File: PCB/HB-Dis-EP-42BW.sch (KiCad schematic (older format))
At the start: 34 parts, among them J1 Reset, J2 FTDI, J3 Conn_ISP, J4 ePaper, J6 Supply, SW0 SW_Push, SW1 SW_Push, SW10 SW_Push, SW2 SW_Push, SW3 SW_Push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

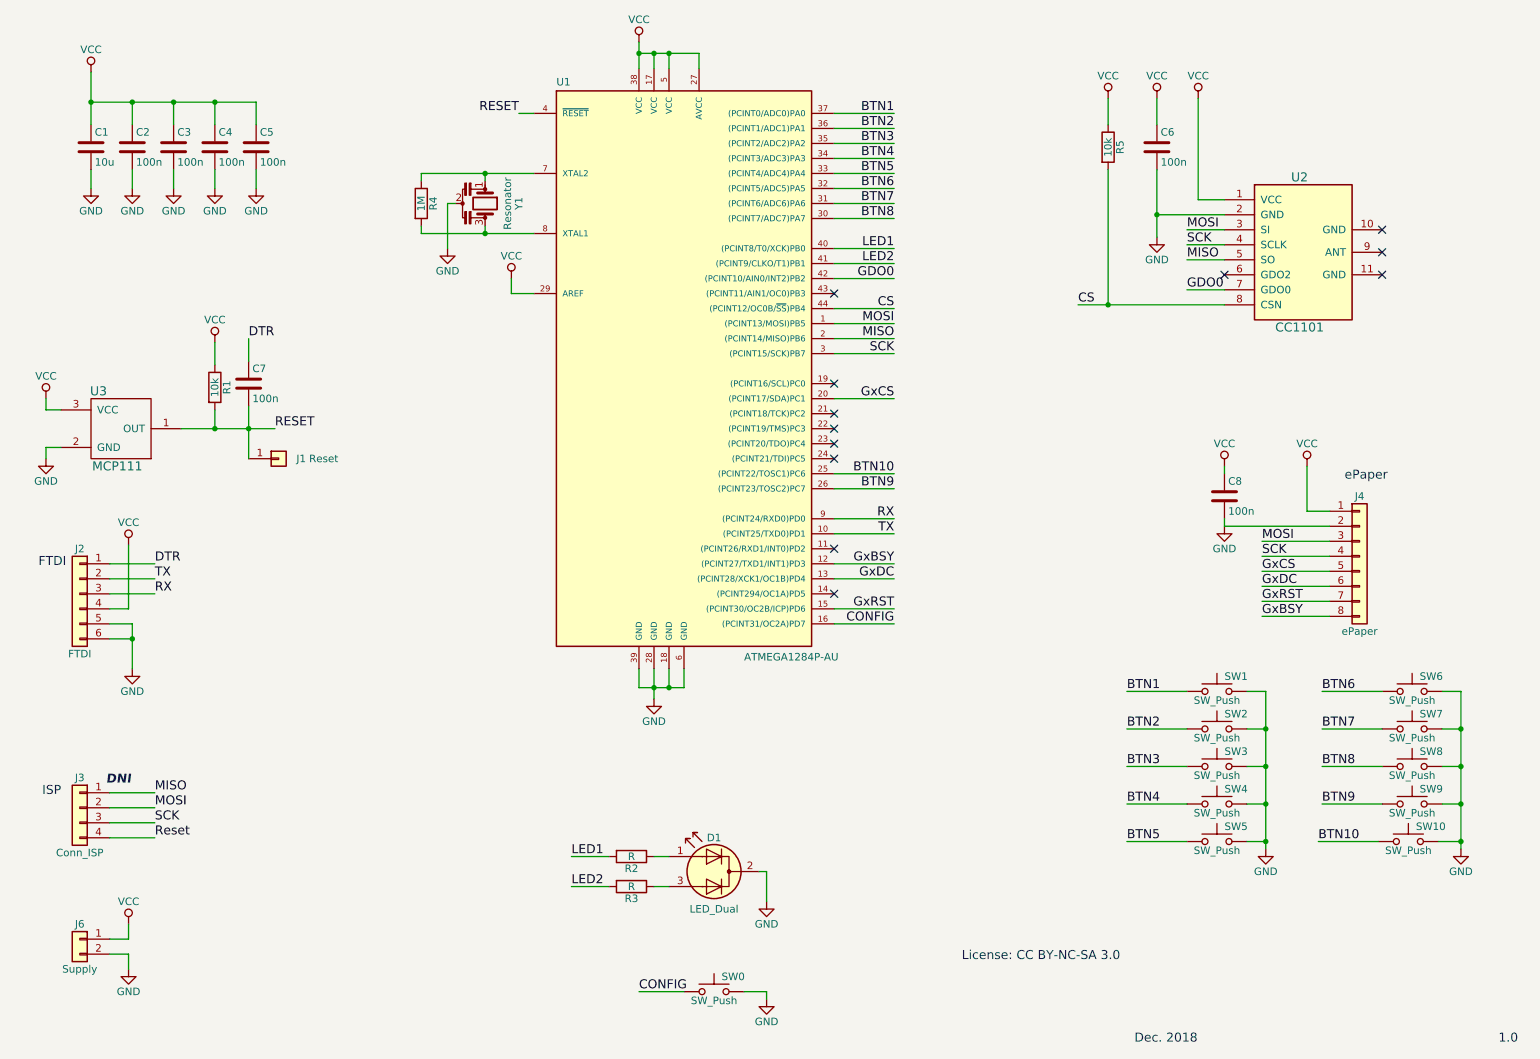
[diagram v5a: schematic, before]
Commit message: several improvement on PCB
- 4x GPIO for future use
- battery measurement under switchable load
- caps @ CC1101 and  @ ePaper changed to 10 uF
- extra solder points on the way to the ePaper connector
  (option to cut the upper 5 mm to fit the size of the bare ePaper)
- remove copper layers in top left, to place antenna there
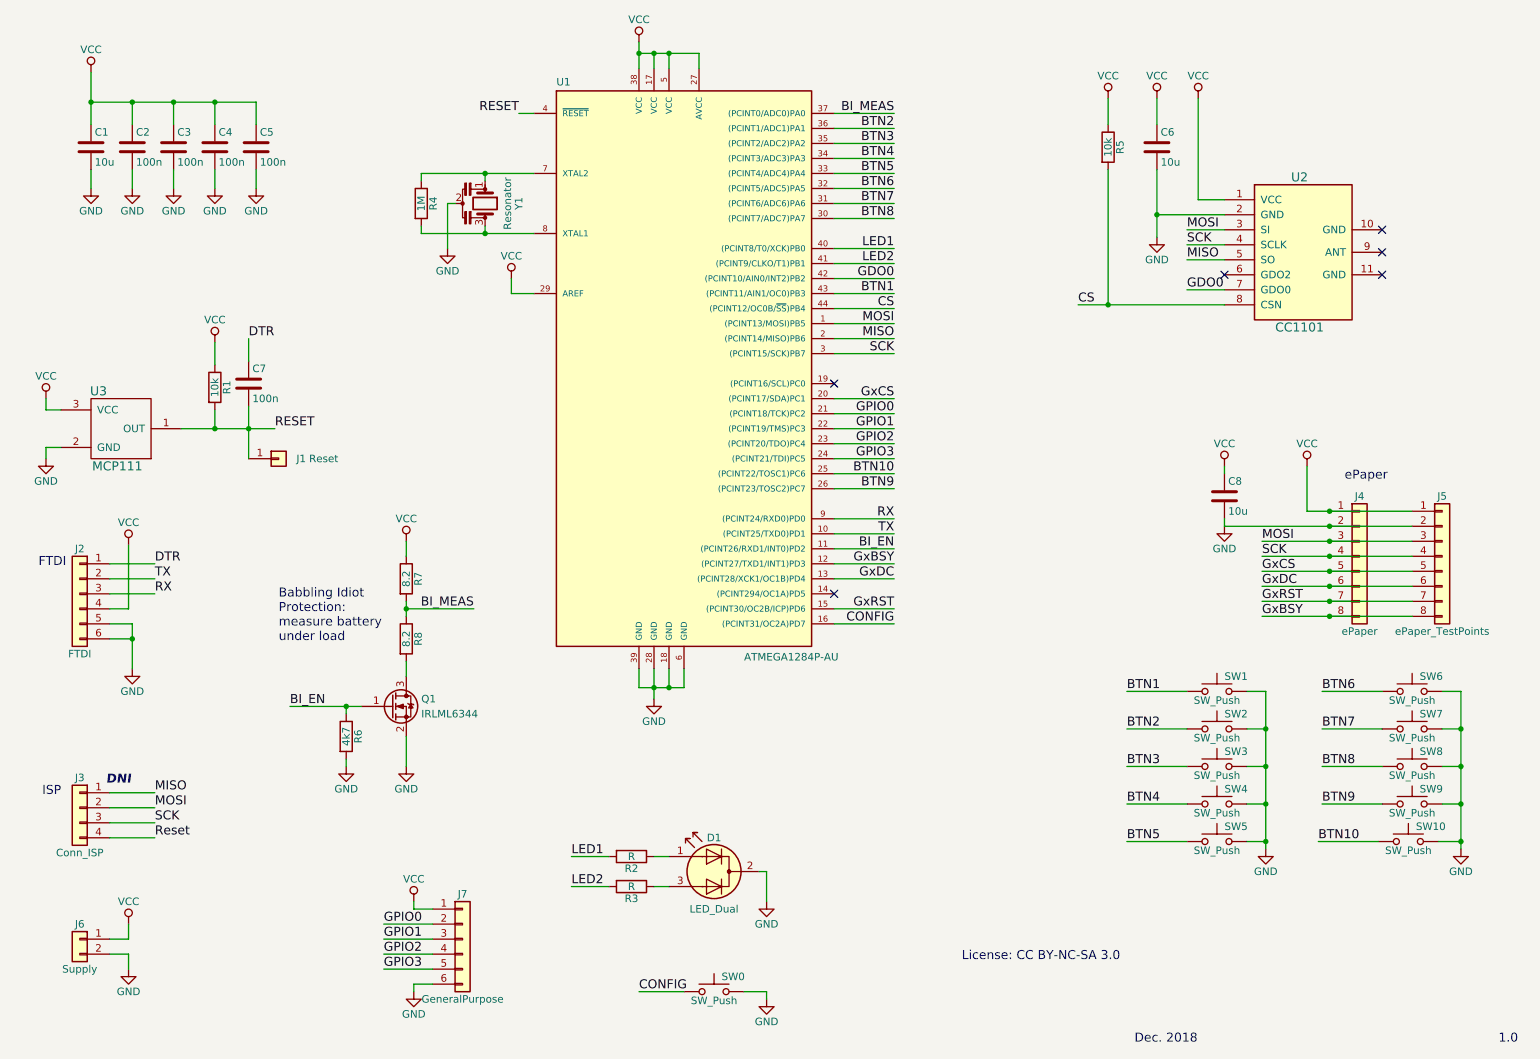
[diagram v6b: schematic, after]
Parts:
- added J5: ePaper_TestPoints, Pin_Headers:Pin_Header_Straight_1x08_Pitch2.54mm, symbol Conn_01x08
- added J7: GeneralPurpose, Pin_Headers:Pin_Header_Straight_1x06_Pitch1.27mm, symbol Conn_01x06
- added Q1: IRLML6344, TO_SOT_Packages_SMD:SOT-23, symbol Q_NMOS_GSD
- added R6: 4k7, Resistors_SMD:R_0603_HandSoldering, symbol R
- added R7, R8: 8.2, Resistors_SMD:R_0603_HandSoldering, symbol R
- C6, C8: value 100n -> 10u
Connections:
- net BTN1: now also U1.43 ((PCINT11/AIN1/OC0)PB3); no longer U1.37 ((PCINT0/ADC0)PA0)
- net GND: now also J5.2 (Pin_2), J7.6 (Pin_6), Q1.2 (S), R6.2
- net GxBSY: now also J5.8 (Pin_8)
- net GxCS: now also J5.5 (Pin_5)
- net GxDC: now also J5.6 (Pin_6)
- net GxRST: now also J5.7 (Pin_7)
- net MOSI: now also J5.3 (Pin_3)
- net SCK: now also J5.4 (Pin_4)
- net VCC: now also J5.1 (Pin_1), J7.1 (Pin_1), R7.1
- net BI_EN: now reaches U1.11 ((PCINT26/RXD1/INT0)PD2)
- net BI_EN: now also Q1.1 (G), R6.1
- net GPIO0: now reaches U1.21 ((PCINT18/TCK)PC2)
- net GPIO0: now also J7.2 (Pin_2)
- net GPIO1: now reaches U1.22 ((PCINT19/TMS)PC3)
- net GPIO1: now also J7.3 (Pin_3)
- net GPIO2: now reaches U1.23 ((PCINT20/TDO)PC4)
- net GPIO2: now also J7.4 (Pin_4)
- net GPIO3: now reaches U1.24 ((PCINT21/TDI)PC5)
- net GPIO3: now also J7.5 (Pin_5)
- new net: Q1.3 (D), R8.2
- new net BI_MEAS: R7.2, R8.1, U1.37 ((PCINT0/ADC0)PA0)
- no-connect marks 12 -> 6
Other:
- note added: "Babbling Idiot \nProtection:\nmeasure battery \nunder load"
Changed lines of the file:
@@
 P 8300 1675
 F 0 "C6" H 8325 1775 50  0000 L CNN
-F 1 "100n" H 8325 1575 50  0000 L CNN
+F 1 "10u" H 8325 1575 50  0000 L CNN
 F 2 "Capacitors_SMD:C_0603_HandSoldering" H 8338 1525 50  0001 C CNN
 F 3 "" H 8300 1675 50  0001 C CNN
@@
 BTN2
 Text Label 6550 1450 2    60   ~ 0
-BTN1
+BI_MEAS
 Text Label 6550 3850 2    60   ~ 0
 BTN10
@@
 Text Label 6550 4750 2    60   ~ 0
 GxRST
-NoConn ~ 6150 2650
-NoConn ~ 6150 3250
-NoConn ~ 6150 3450
-NoConn ~ 6150 3550
-NoConn ~ 6150 3650
-NoConn ~ 6150 3750
-NoConn ~ 6150 4350
 NoConn ~ 6150 4650
 $Comp
@@
 $EndComp
 Wire Wire Line
-	9450 4500 9000 4500
-Wire Wire Line
-	9000 4600 9450 4600
-Wire Wire Line
-	9450 4700 9000 4700
-Wire Wire Line
-	9000 4800 9450 4800
+	9000 4500 10000 4500
+Wire Wire Line
+	9000 4600 10000 4600
+Wire Wire Line
+	9000 4700 10000 4700
+Wire Wire Line
+	9000 4800 10000 4800
 Text Label 9000 4500 0    60   ~ 0
 GxCS
@@
 $EndComp
 Wire Wire Line
-	9450 4200 8750 4200
+	8750 4200 10000 4200
 $Comp
 L VCC #PWR017
@@
 P 8750 4000
 F 0 "C8" H 8775 4100 50  0000 L CNN
-F 1 "100n" H 8775 3900 50  0000 L CNN
+F 1 "10u" H 8775 3900 50  0000 L CNN
 F 2 "Capacitors_SMD:C_0603_HandSoldering" H 8788 3850 50  0001 C CNN
 F 3 "" H 8750 4000 50  0001 C CNN
@@
 	9300 3800 9300 4100
 Wire Wire Line
-	9300 4100 9450 4100
+	9300 4100 10000 4100
 Text Notes 9550 3900 0    60   ~ 0
 ePaper
@@
 $EndComp
 Wire Wire Line
-	9450 4400 9000 4400
-Wire Wire Line
-	9000 4300 9450 4300
+	9000 4400 10000 4400
+Wire Wire Line
+	9000 4300 10000 4300
 Text Label 9000 4300 0    60   ~ 0
 MOSI
@@
 	1    0    0    -1
 $EndComp
+Wire Wire Line
+	6150 3450 6550 3450
+Wire Wire Line
+	6550 3550 6150 3550
+Wire Wire Line
+	6150 3650 6550 3650
+Wire Wire Line
+	6550 3750 6150 3750
+Text Label 6550 3450 2    60   ~ 0
+GPIO0
+Text Label 6550 3550 2    60   ~ 0
+GPIO1
+Text Label 6550 3650 2    60   ~ 0
+GPIO2
+Text Label 6550 3750 2    60   ~ 0
+GPIO3
+$Comp
+L Conn_01x06 J7
+U 1 1 5C3A1225
+P 3675 6950
+F 0 "J7" H 3675 7250 50  0000 C CNN
+F 1 "GeneralPurpose" H 3675 6550 50  0000 C CNN
+F 2 "Pin_Headers:Pin_Header_Straight_1x06_Pitch1.27mm" H 3675 6950 50  0001 C CNN
+F 3 "" H 3675 6950 50  0001 C CNN
+	1    3675 6950
+	1    0    0    -1
+$EndComp
+$Comp
+L GND #PWR029
+U 1 1 5C3A1499
+P 3350 7300
+F 0 "#PWR029" H 3350 7050 50  0001 C CNN
+F 1 "GND" H 3350 7150 50  0000 C CNN
+F 2 "" H 3350 7300 50  0001 C CNN
+F 3 "" H 3350 7300 50  0001 C CNN
+	1    3350 7300
+	1    0    0    -1
+$EndComp
+$Comp
+L VCC #PWR030
+U 1 1 5C3A150D
+P 3350 6700
+F 0 "#PWR030" H 3350 6550 50  0001 C CNN
+F 1 "VCC" H 3350 6850 50  0000 C CNN
+F 2 "" H 3350 6700 50  0001 C CNN
+F 3 "" H 3350 6700 50  0001 C CNN
+	1    3350 6700
+	1    0    0    -1
+$EndComp
+Wire Wire Line
+	3350 7300 3350 7250
+Wire Wire Line
+	3350 7250 3475 7250
+Wire Wire Line
+	3350 6700 3350 6750
+Wire Wire Line
+	3350 6750 3475 6750
+Wire Wire Line
+	3475 6850 3150 6850
+Text Label 3150 6850 0    60   ~ 0
+GPIO0
+Wire Wire Line
+	3475 6950 3150 6950
+Wire Wire Line
+	3475 7050 3150 7050
+Wire Wire Line
+	3150 7150 3475 7150
+Text Label 3150 6950 0    60   ~ 0
+GPIO1
+Text Label 3150 7050 0    60   ~ 0
+GPIO2
+Text Label 3150 7150 0    60   ~ 0
+GPIO3
+$Comp
+L Conn_01x08 J5
+U 1 1 5C3A255F
+P 10200 4400
+F 0 "J5" H 10200 4800 50  0000 C CNN
+F 1 "ePaper_TestPoints" H 10200 3900 50  0000 C CNN
+F 2 "Pin_Headers:Pin_Header_Straight_1x08_Pitch2.54mm" H 10200 4400 50  0001 C CNN
+F 3 "" H 10200 4400 50  0001 C CNN
+	1    10200 4400
+	1    0    0    -1
+$EndComp
+Connection ~ 9450 4100
+Connection ~ 9450 4200
+Connection ~ 9450 4300
+Connection ~ 9450 4400
+Connection ~ 9450 4500
+Connection ~ 9450 4600
+Connection ~ 9450 4700
+Connection ~ 9450 4800
+$Comp
+L Q_NMOS_GSD Q1
+U 1 1 5C3A3284
+P 3200 5400
+F 0 "Q1" H 3400 5450 50  0000 L CNN
+F 1 "IRLML6344" H 3400 5350 50  0000 L CNN
+F 2 "TO_SOT_Packages_SMD:SOT-23" H 3400 5500 50  0001 C CNN
+F 3 "" H 3200 5400 50  0001 C CNN
+	1    3200 5400
+	1    0    0    -1
+$EndComp
+$Comp
+L R R8
+U 1 1 5C3A3483
+P 3300 4950
+F 0 "R8" V 3380 4950 50  0000 C CNN
+F 1 "8.2" V 3300 4950 50  0000 C CNN
+F 2 "Resistors_SMD:R_0603_HandSoldering" V 3230 4950 50  0001 C CNN
+F 3 "" H 3300 4950 50  0001 C CNN
+	1    3300 4950
+	1    0    0    -1
+$EndComp
+$Comp
+L R R7
+U 1 1 5C3A3574
+P 3300 4550
+F 0 "R7" V 3380 4550 50  0000 C CNN
+F 1 "8.2" V 3300 4550 50  0000 C CNN
+F 2 "Resistors_SMD:R_0603_HandSoldering" V 3230 4550 50  0001 C CNN
+F 3 "" H 3300 4550 50  0001 C CNN
+	1    3300 4550
+	1    0    0    -1
+$EndComp
+$Comp
+L GND #PWR031
+U 1 1 5C3A369E
+P 3300 5800
+F 0 "#PWR031" H 3300 5550 50  0001 C CNN
+F 1 "GND" H 3300 5650 50  0000 C CNN
+F 2 "" H 3300 5800 50  0001 C CNN
+F 3 "" H 3300 5800 50  0001 C CNN
+	1    3300 5800
+	1    0    0    -1
+$EndComp
+Wire Wire Line
+	3300 5600 3300 5800
+Wire Wire Line
+	3300 5100 3300 5200
+Wire Wire Line
+	3300 4700 3300 4800
+$Comp
+L VCC #PWR032
+U 1 1 5C3A3BF5
+P 3300 4300
+F 0 "#PWR032" H 3300 4150 50  0001 C CNN
+F 1 "VCC" H 3300 4450 50  0000 C CNN
+F 2 "" H 3300 4300 50  0001 C CNN
+F 3 "" H 3300 4300 50  0001 C CNN
+	1    3300 4300
+	1    0    0    -1
+$EndComp
+Wire Wire Line
+	3300 4300 3300 4400
+$Comp
+L R R6
+U 1 1 5C3A3E02
+P 2900 5600
+F 0 "R6" V 2980 5600 50  0000 C CNN
+F 1 "4k7" V 2900 5600 50  0000 C CNN
+F 2 "Resistors_SMD:R_0603_HandSoldering" V 2830 5600 50  0001 C CNN
+F 3 "" H 2900 5600 50  0001 C CNN
+	1    2900 5600
+	1    0    0    -1
+$EndComp
+Wire Wire Line
+	2525 5400 3000 5400
+Wire Wire Line
+	2900 5450 2900 5400
+Connection ~ 2900 5400
+Wire Wire Line
+	3300 4750 3750 4750
+Connection ~ 3300 4750
+Text Label 2525 5400 0    60   ~ 0
+BI_EN
+Text Label 3750 4750 2    60   ~ 0
+BI_MEAS
+$Comp
+L GND #PWR033
+U 1 1 5C3A45E4
+P 2900 5800
+F 0 "#PWR033" H 2900 5550 50  0001 C CNN
+F 1 "GND" H 2900 5650 50  0000 C CNN
+F 2 "" H 2900 5800 50  0001 C CNN
+F 3 "" H 2900 5800 50  0001 C CNN
+	1    2900 5800
+	1    0    0    -1
+$EndComp
+Wire Wire Line
+	2900 5800 2900 5750
+Text Label 6550 4350 2    60   ~ 0
+BI_EN
+Wire Wire Line
+	6150 2650 6550 2650
+Text Label 6550 2650 2    60   ~ 0
+BTN1
+Text Notes 2450 4975 0    60   ~ 0
+Babbling Idiot \nProtection:\nmeasure battery \nunder load
+Wire Wire Line
+	6150 4350 6550 4350
+NoConn ~ 6150 3250
 $EndSCHEMATC

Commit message: further improvements to PCB
- change caps @ CC1101 and @ ePaper to 1 uF
- shrink GPIOs to 3
- add I²C connecter for future use
- move config button to desired place and add hole for optional head-over-heels mounting
- add 6-pin JTAG header on backside
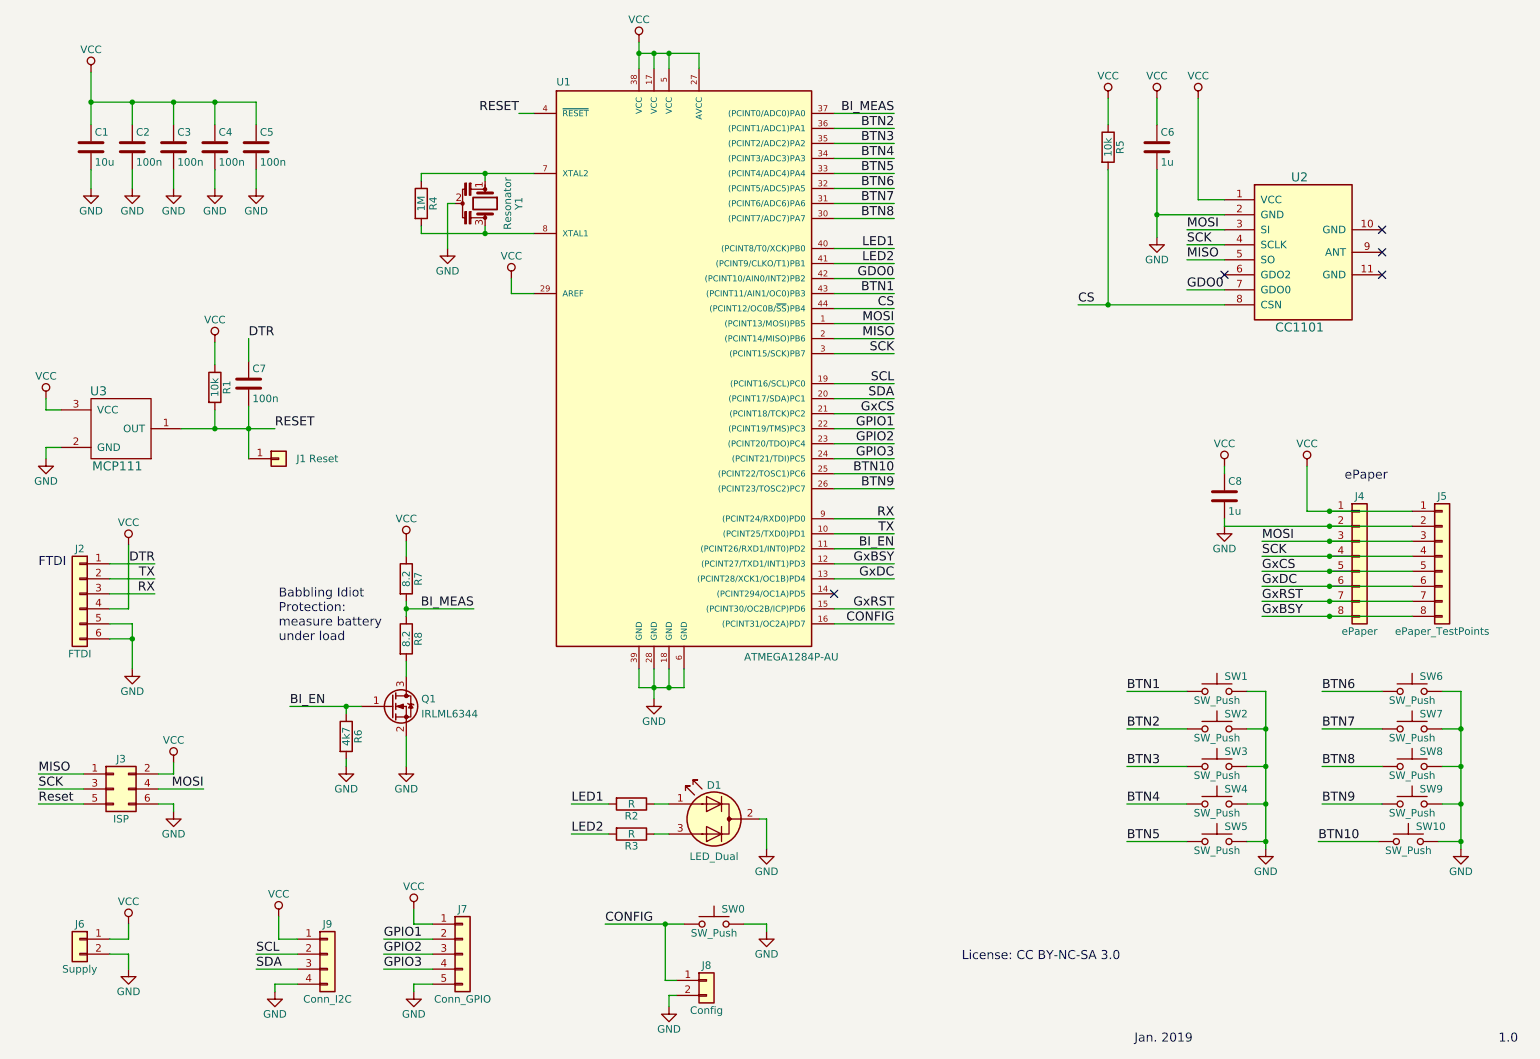
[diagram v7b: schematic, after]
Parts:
- removed J3: Conn_ISP, Pin_Headers:Pin_Header_Straight_1x04_Pitch2.54mm, symbol Conn_01x04
- removed J7: GeneralPurpose, Pin_Headers:Pin_Header_Straight_1x06_Pitch1.27mm, symbol Conn_01x06
- added J3: ISP, Pin_Headers:Pin_Header_Straight_2x03_Pitch2.54mm, symbol Conn_02x03_Odd_Even
- added J7: Conn_GPIO, Pin_Headers:Pin_Header_Straight_1x05_Pitch1.27mm, symbol Conn_01x05
- added J8: Config, Pin_Headers:Pin_Header_Straight_1x02_Pitch2.54mm, symbol Conn_01x02
- added J9: Conn_I2C, Pin_Headers:Pin_Header_Straight_1x04_Pitch1.27mm, symbol Conn_01x04
- C6, C8: value 10u -> 1u
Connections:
- net GPIO0 is gone; now on net GxCS: U1.21 ((PCINT18/TCK)PC2)
- net CONFIG: now also J8.1 (Pin_1)
- net GND: now also J3.6 (Pin_6), J7.5 (Pin_5), J8.2 (Pin_2), J9.4 (Pin_4)
- net GPIO1: now also J7.2 (Pin_2)
- net GPIO2: now also J7.3 (Pin_3)
- net GPIO3: now also J7.4 (Pin_4)
- net GxCS: no longer U1.20 ((PCINT17/SDA)PC1)
- net MISO: now also J3.1 (Pin_1)
- net MOSI: now also J3.4 (Pin_4)
- net Reset: now also J3.5 (Pin_5)
- net SCK: now also J3.3 (Pin_3)
- net VCC: now also J3.2 (Pin_2), J7.1 (Pin_1), J9.1 (Pin_1)
- net SCL: now reaches U1.19 ((PCINT16/SCL)PC0)
- net SCL: now also J9.2 (Pin_2)
- new net SDA: J9.3 (Pin_3), U1.20 ((PCINT17/SDA)PC1)
- no-connect marks 6 -> 5
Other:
- note added: "Jan. 2019"
- note removed: "DNI"
- note removed: "Dec. 2018"
- note removed: "ISP"
- moved on the sheet: D1, R2, R3, SW0

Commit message: even more improvements on PCB
- slimmer pads on TQFP44 for easier soldering
- CC1101 power pads changed to "oval" so that the net is connected horizontal/vertical and not diagonal
- moved vias out of SMD pads
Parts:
- U1: footprint Housings_QFP:TQFP-44_10x10mm_Pitch0.8mm -> TQFP Housings:TQFP-44_10x10mm_Pitch0.8mm_HandSoldering
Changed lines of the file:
@@
 F 0 "U1" H 4300 5030 50  0000 L BNN
 F 1 "ATMEGA1284P-AU" H 5550 1200 50  0000 L BNN
-F 2 "Housings_QFP:TQFP-44_10x10mm_Pitch0.8mm" H 5150 3150 50  0001 C CIN
+F 2 "TQFP Housings:TQFP-44_10x10mm_Pitch0.8mm_HandSoldering" H 5150 3150 50  0001 C CIN
 F 3 "" H 5150 3150 50  0001 C CNN
 	1    5150 3150
